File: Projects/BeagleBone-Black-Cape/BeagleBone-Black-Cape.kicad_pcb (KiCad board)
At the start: 2 copper layers, 86.4 x 54.6 mm, 6 parts, among them P8 BeagleBone_Black_Header, P9 BeagleBone_Black_Header

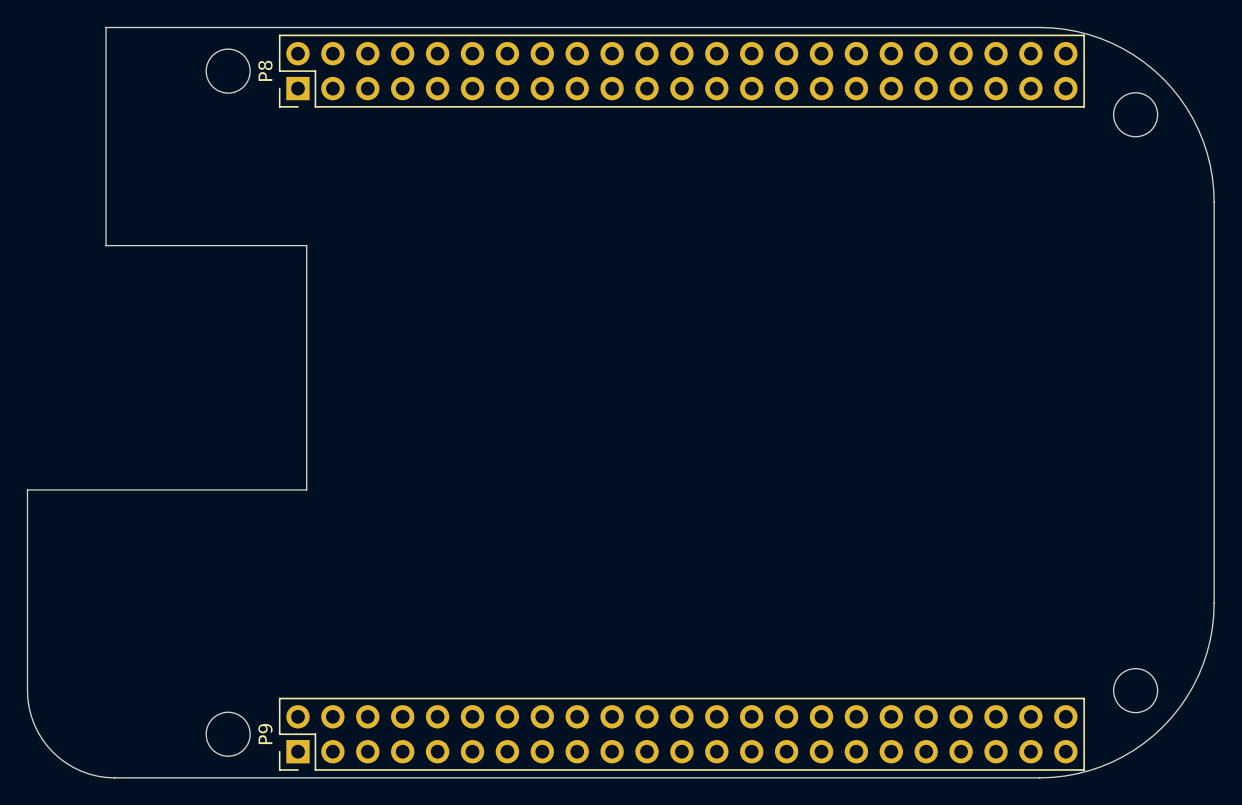
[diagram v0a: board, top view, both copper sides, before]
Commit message: adding parts placer position file
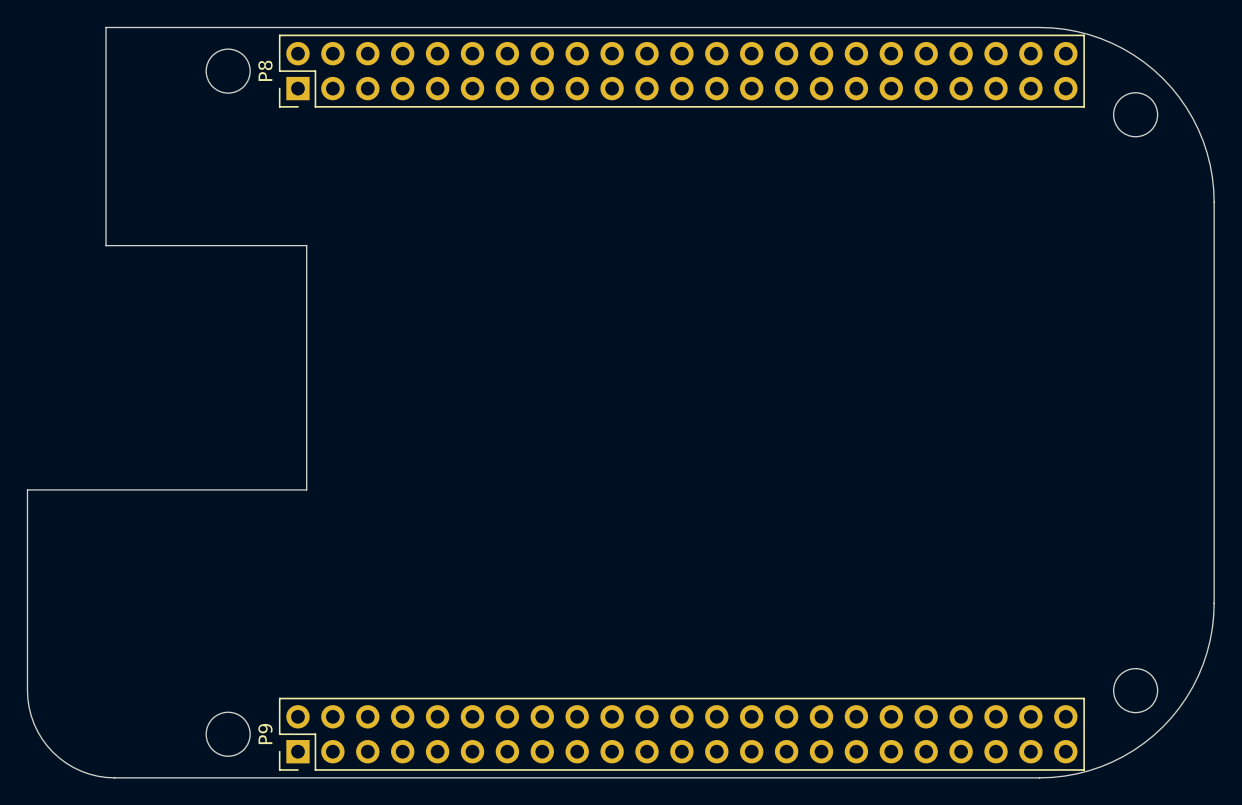
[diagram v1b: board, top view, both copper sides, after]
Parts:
- added BOARD: board, Library:board, F.Cu at (143.2, 72.7)
